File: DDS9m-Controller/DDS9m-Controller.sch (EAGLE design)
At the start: 15 parts, among them IC1 LTC6994-X, IC3 74LVC1G07DCK, X1 BNC-V

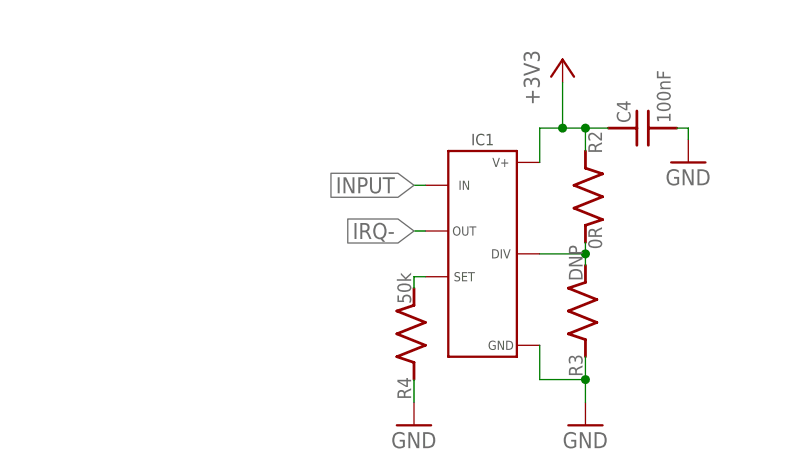
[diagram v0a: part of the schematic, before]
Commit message: Finished test layout
First pass at the schematic and board is ready to prototype.

DSB
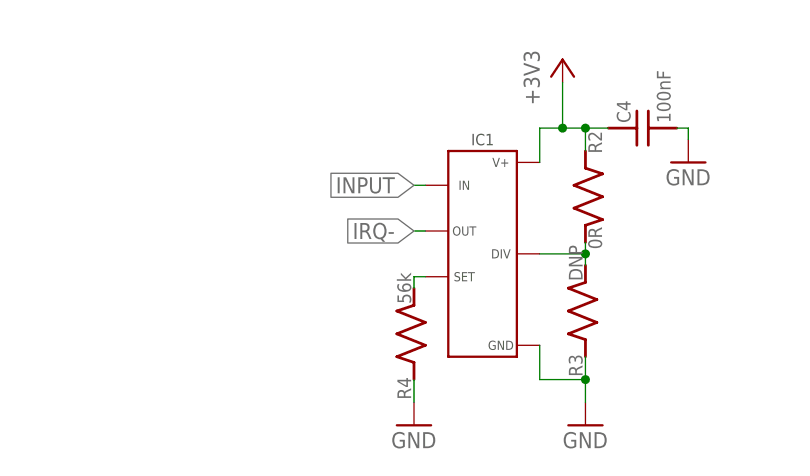
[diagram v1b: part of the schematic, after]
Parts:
- C1: PARTNO (none) -> CL05C220JB51PNC
- C2, C4, C5: PARTNO (none) -> CL10B104KB8NNNC
- C3: PARTNO (none) -> CL32B106KLJNNNE
- R1: PARTNO (none) -> ERJ-3EKF3320V
- R2: PARTNO (none) -> MF-RES-0603-0
- R4: value 50k -> 56k; PARTNO (none) -> ERA-3AEB563V
- R5: PARTNO (none) -> ERJ-3EKF3301V
- X1: PARTNO (none) -> 5227222-3
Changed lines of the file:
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@@
 <part name="+3V1" library="supply1" library_urn="urn:adsk.eagle:library:371" deviceset="+3V3" device=""/>
 <part name="GND1" library="supply1" library_urn="urn:adsk.eagle:library:371" deviceset="GND" device=""/>
-<part name="R1" library="jqi_passives" deviceset="R_SMD" device="R0603" value="332"/>
-<part name="C1" library="jqi_passives" deviceset="C_MLCC_SMD" device="CMLCC_0402" value="22pF"/>
+<part name="R1" library="jqi_passives" deviceset="R_SMD" device="R0603" value="332">
+<attribute name="PARTNO" value="ERJ-3EKF3320V"/>
+</part>
+<part name="C1" library="jqi_passives" deviceset="C_MLCC_SMD" device="CMLCC_0402" value="22pF">
+<attribute name="PARTNO" value="CL05C220JB51PNC"/>
+</part>
 <part name="+3V2" library="supply1" library_urn="urn:adsk.eagle:library:371" deviceset="+3V3" device=""/>
 <part name="+3V3" library="supply1" library_urn="urn:adsk.eagle:library:371" deviceset="+3V3" device=""/>
-<part name="R2" library="jqi_passives" deviceset="R_SMD" device="R0603" value="0R"/>
+<part name="R2" library="jqi_passives" deviceset="R_SMD" device="R0603" value="0R">
+<attribute name="PARTNO" value="MF-RES-0603-0"/>
+</part>
 <part name="R3" library="jqi_passives" deviceset="R_SMD" device="R0603" value="DNP"/>
-<part name="R4" library="jqi_passives" deviceset="R_SMD" device="R0603" value="50k"/>
-<part name="C2" library="jqi_passives" deviceset="C_MLCC_SMD" device="CMLCC_0603" value="100nF"/>
-<part name="X1" library="connector-jqi" deviceset="BNC" device="-V"/>
-<part name="C3" library="jqi_passives" deviceset="C_MLCC_SMD" device="CMLCC_1210" value="10uF"/>
-<part name="C4" library="jqi_passives" deviceset="C_MLCC_SMD" device="CMLCC_0603" value="100nF"/>
+<part name="R4" library="jqi_passives" deviceset="R_SMD" device="R0603" value="56k">
+<attribute name="PARTNO" value="ERA-3AEB563V"/>
+</part>
+<part name="C2" library="jqi_passives" deviceset="C_MLCC_SMD" device="CMLCC_0603" value="100nF">
+<attribute name="PARTNO" value="CL10B104KB8NNNC"/>
+</part>
+<part name="X1" library="connector-jqi" deviceset="BNC" device="-V">
+<attribute name="PARTNO" value="5227222-3"/>
+</part>
+<part name="C3" library="jqi_passives" deviceset="C_MLCC_SMD" device="CMLCC_1210" value="10uF">
+<attribute name="PARTNO" value="CL32B106KLJNNNE"/>
+</part>
+<part name="C4" library="jqi_passives" deviceset="C_MLCC_SMD" device="CMLCC_0603" value="100nF">
+<attribute name="PARTNO" value="CL10B104KB8NNNC"/>
+</part>
 <part name="GND2" library="supply1" library_urn="urn:adsk.eagle:library:371" deviceset="GND" device=""/>
 <part name="GND3" library="supply1" library_urn="urn:adsk.eagle:library:371" deviceset="GND" device=""/>
@@
 <attribute name="PARTNO" value="SN74LVC1G07DCKR"/>
 </part>
-<part name="C5" library="jqi_passives" deviceset="C_MLCC_SMD" device="CMLCC_0603" value="100nF"/>
+<part name="C5" library="jqi_passives" deviceset="C_MLCC_SMD" device="CMLCC_0603" value="100nF">
+<attribute name="PARTNO" value="CL10B104KB8NNNC"/>
+</part>
 <part name="GND5" library="supply1" library_urn="urn:adsk.eagle:library:371" deviceset="GND" device=""/>
-<part name="R5" library="jqi_passives" deviceset="R_SMD" device="R0603" value="3.3k"/>
+<part name="R5" library="jqi_passives" deviceset="R_SMD" device="R0603" value="3.3k">
+<attribute name="PARTNO" value="ERJ-3EKF3301V"/>
+</part>
 <part name="+3V4" library="supply1" library_urn="urn:adsk.eagle:library:371" deviceset="+3V3" device=""/>
 <part name="GND6" library="supply1" library_urn="urn:adsk.eagle:library:371" deviceset="GND" device=""/>
@@
 <attribute name="NAME" x="32.0675" y="185.7375" size="1.524" layer="95"/>
 <attribute name="VALUE" x="42.7038" y="185.7375" size="1.524" layer="96"/>
+<attribute name="PARTNO" x="39.37" y="185.42" size="1.778" layer="96" display="off"/>
 </instance>
 <instance part="C1" gate="G$1" x="40.64" y="181.61" smashed="yes" rot="R270">
 <attribute name="NAME" x="40.7035" y="181.0385" size="1.524" layer="95" rot="R270"/>
 <attribute name="VALUE" x="36.2585" y="181.0385" size="1.524" layer="96" rot="R270"/>
+<attribute name="PARTNO" x="40.64" y="181.61" size="1.778" layer="96" display="off"/>
 </instance>
 <instance part="+3V2" gate="G$1" x="69.85" y="201.93" smashed="yes">
@@
 <attribute name="NAME" x="134.9375" y="143.1925" size="1.524" layer="95" rot="R270"/>
 <attribute name="VALUE" x="134.9375" y="132.5562" size="1.524" layer="96" rot="R270"/>
+<attribute name="PARTNO" x="134.62" y="135.89" size="1.778" layer="96" display="off"/>
 </instance>
 <instance part="R3" gate="G$1" x="134.62" y="123.19" smashed="yes" rot="R90">
@@
 <attribute name="NAME" x="115.2525" y="113.3475" size="1.524" layer="95" rot="R90"/>
 <attribute name="VALUE" x="115.2525" y="123.9838" size="1.524" layer="96" rot="R90"/>
+<attribute name="PARTNO" x="115.57" y="120.65" size="1.778" layer="96" display="off"/>
 </instance>
 <instance part="C2" gate="G$1" x="73.66" y="198.12" smashed="yes" rot="R90">
 <attribute name="NAME" x="73.5965" y="198.6915" size="1.524" layer="95" rot="R90"/>
 <attribute name="VALUE" x="78.0415" y="198.6915" size="1.524" layer="96" rot="R90"/>
+<attribute name="PARTNO" x="73.66" y="198.12" size="1.778" layer="96" display="off"/>
 </instance>
 <instance part="X1" gate="G$1" x="26.67" y="190.5" smashed="yes">
 <attribute name="NAME" x="24.13" y="193.802" size="1.778" layer="95"/>
+<attribute name="PARTNO" x="26.67" y="190.5" size="1.778" layer="96" display="off"/>
 </instance>
 <instance part="C3" gate="G$1" x="195.58" y="189.23" smashed="yes">
 <attribute name="NAME" x="196.1515" y="189.2935" size="1.524" layer="95"/>
 <attribute name="VALUE" x="196.1515" y="184.8485" size="1.524" layer="96"/>
+<attribute name="PARTNO" x="195.58" y="189.23" size="1.778" layer="96" display="off"/>
 </instance>
 <instance part="C4" gate="G$1" x="139.7" y="143.51" smashed="yes" rot="R90">
 <attribute name="NAME" x="139.6365" y="144.0815" size="1.524" layer="95" rot="R90"/>
 <attribute name="VALUE" x="144.0815" y="144.0815" size="1.524" layer="96" rot="R90"/>
+<attribute name="PARTNO" x="139.7" y="143.51" size="1.778" layer="96" display="off"/>
 </instance>
 <instance part="GND2" gate="1" x="195.58" y="180.34" smashed="yes">
@@
 <attribute name="NAME" x="83.7565" y="198.6915" size="1.524" layer="95" rot="R90"/>
 <attribute name="VALUE" x="88.2015" y="198.6915" size="1.524" layer="96" rot="R90"/>
+<attribute name="PARTNO" x="83.82" y="198.12" size="1.778" layer="96" display="off"/>
 </instance>
 <instance part="GND5" gate="1" x="96.52" y="176.53" smashed="yes">
@@
 <attribute name="NAME" x="99.3775" y="198.4375" size="1.524" layer="95"/>
 <attribute name="VALUE" x="110.0138" y="198.4375" size="1.524" layer="96"/>
+<attribute name="PARTNO" x="106.68" y="198.12" size="1.778" layer="96" display="off"/>
 </instance>
 <instance part="+3V4" gate="G$1" x="96.52" y="201.93" smashed="yes">
